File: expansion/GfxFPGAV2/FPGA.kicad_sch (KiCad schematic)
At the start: 26 parts, among them J1 JTAG, U2 XC6SLX9-FTG256, U302 W25Q64JVSSIM, Y1 ECS-3963

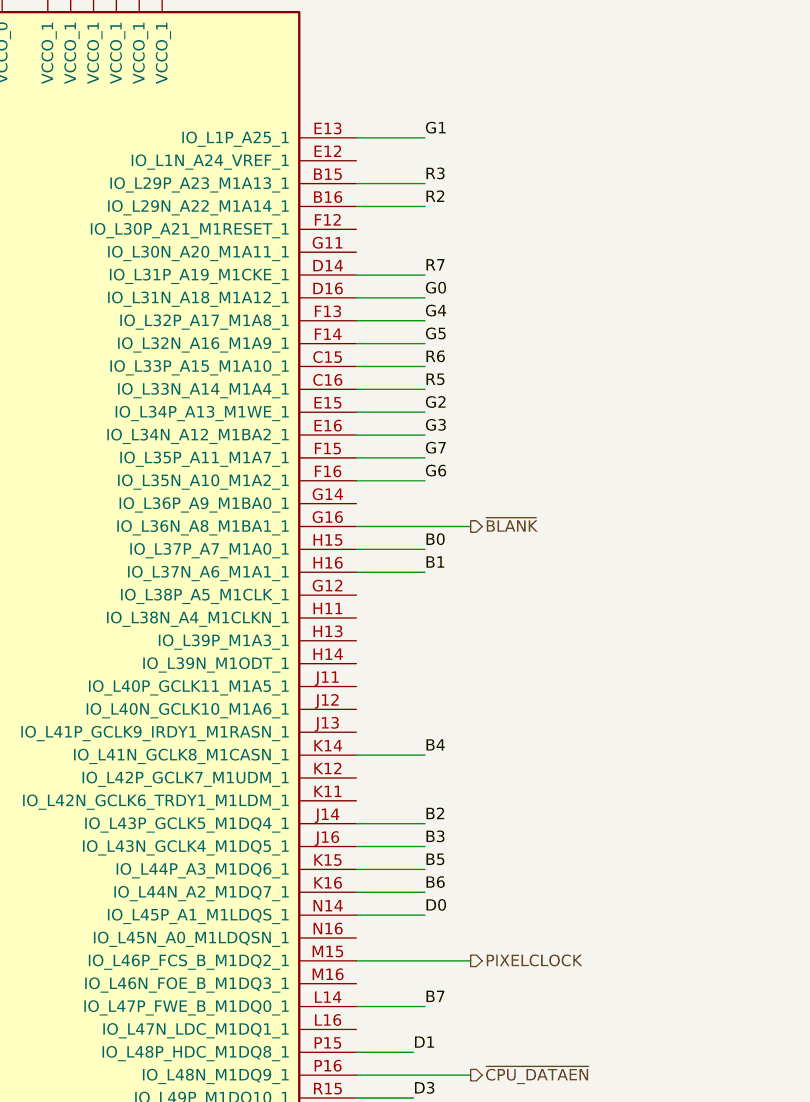
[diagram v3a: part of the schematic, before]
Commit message: Working on VGA baord layout
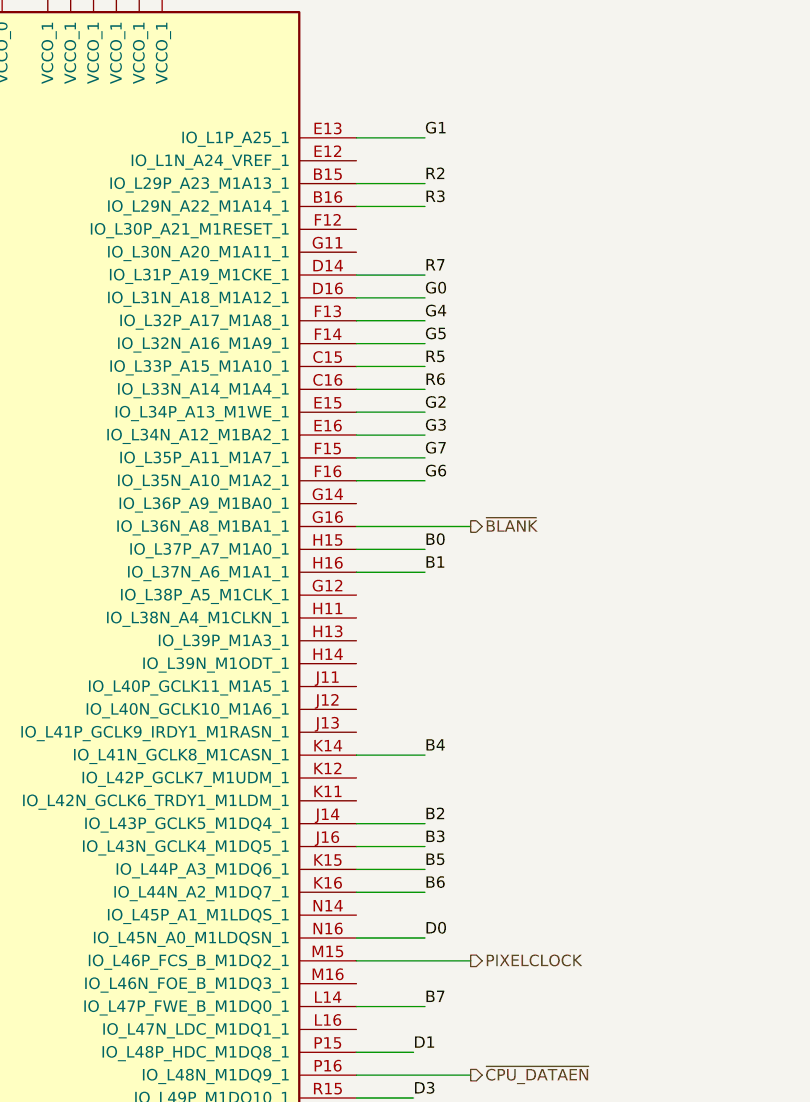
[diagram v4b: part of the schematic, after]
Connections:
- net D0: now also U2.N16 (IO_L45N_A0_M1LDQSN_1); no longer U2.N14 (IO_L45P_A1_M1LDQS_1)
- net R2: now also U2.B15 (IO_L29P_A23_M1A13_1); no longer U2.B16 (IO_L29N_A22_M1A14_1)
- net R3: now also U2.B16 (IO_L29N_A22_M1A14_1); no longer U2.B15 (IO_L29P_A23_M1A13_1)
- net R5: now also U2.C15 (IO_L33P_A15_M1A10_1); no longer U2.C16 (IO_L33N_A14_M1A4_1)
- net R6: now also U2.C16 (IO_L33N_A14_M1A4_1); no longer U2.C15 (IO_L33P_A15_M1A10_1)
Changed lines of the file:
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@@
 	(wire
 		(pts
-			(xy 152.4 130.81) (xy 144.78 130.81)
+			(xy 152.4 133.35) (xy 144.78 133.35)
 		)
 		(stroke
@@
 	)
 	(label "R2"
-		(at 152.4 52.07 0)
+		(at 152.4 49.53 0)
 		(fields_autoplaced yes)
 		(effects
@@
 	)
 	(label "R6"
-		(at 152.4 69.85 0)
+		(at 152.4 72.39 0)
 		(fields_autoplaced yes)
 		(effects
@@
 	)
 	(label "R3"
-		(at 152.4 49.53 0)
+		(at 152.4 52.07 0)
 		(fields_autoplaced yes)
 		(effects
@@
 	)
 	(label "D0"
-		(at 152.4 130.81 0)
+		(at 152.4 133.35 0)
 		(fields_autoplaced yes)
 		(effects
@@
 	)
 	(label "R5"
-		(at 152.4 72.39 0)
+		(at 152.4 69.85 0)
 		(fields_autoplaced yes)
 		(effects

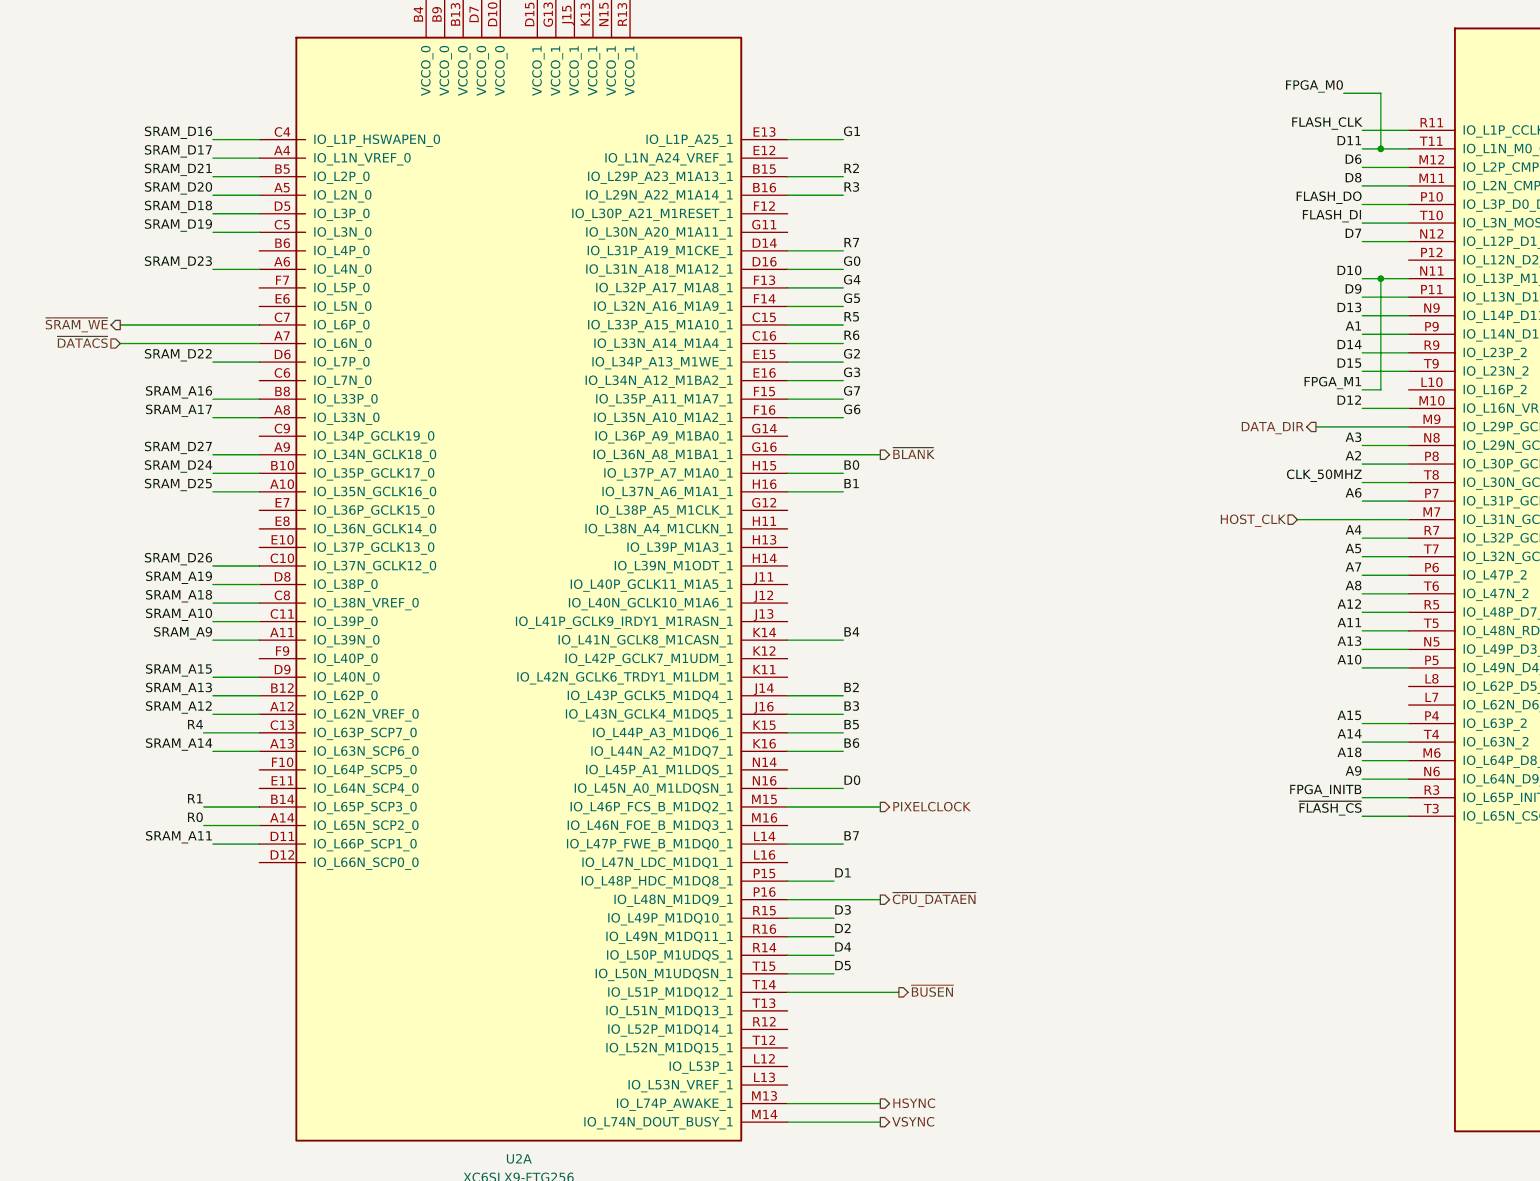
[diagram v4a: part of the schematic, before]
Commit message: More routing on the VGA board
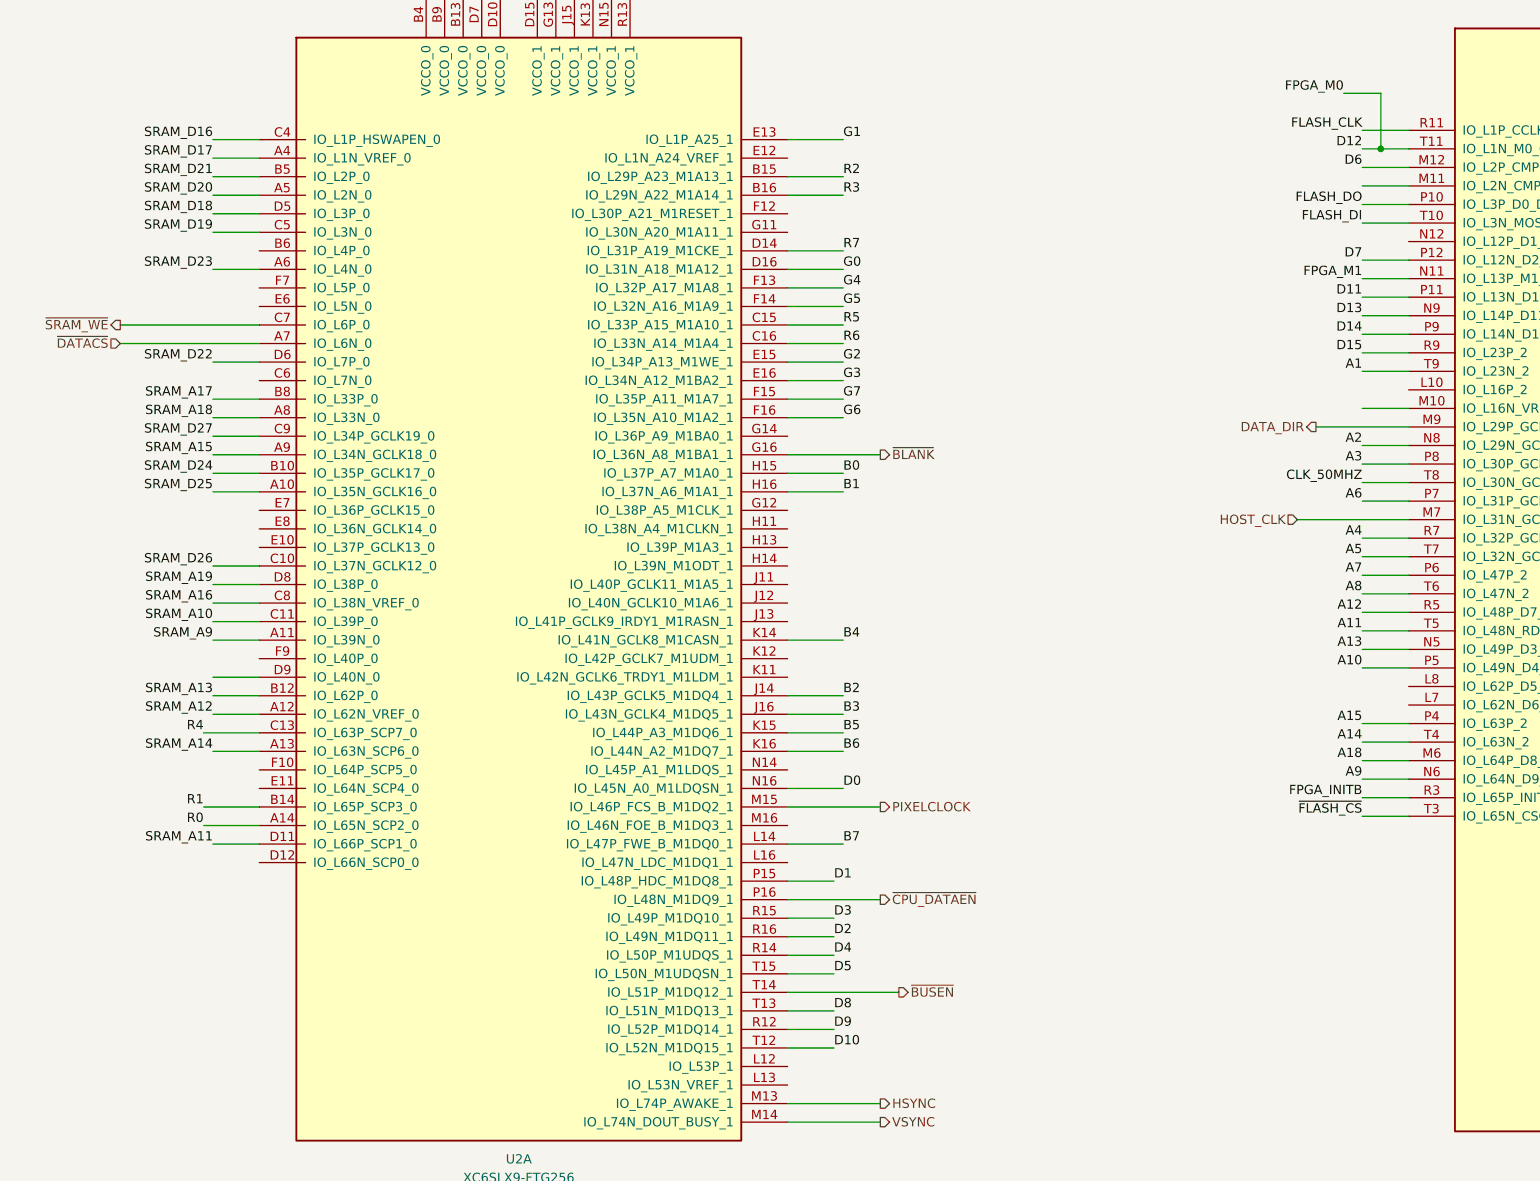
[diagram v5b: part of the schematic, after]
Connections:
- net A1: now also U2.T9 (IO_L23N_2); no longer U2.P9 (IO_L14N_D12_2)
- net A2: now also U2.N8 (IO_L29N_GCLK2_2); no longer U2.P8 (IO_L30P_GCLK1_D13_2)
- net A3: now also U2.P8 (IO_L30P_GCLK1_D13_2); no longer U2.N8 (IO_L29N_GCLK2_2)
- net D10: now also U2.T12 (IO_L52N_M1DQ15_1); no longer R1.1, U2.N11 (IO_L13P_M1_2)
- net D11: now also U2.P11 (IO_L13N_D10_2); no longer R4.2, U2.T11 (IO_L1N_M0_CMPMISO_2)
- net D12: now also R4.2, U2.T11 (IO_L1N_M0_CMPMISO_2); no longer U2.M10 (IO_L16N_VREF_2)
- net D14: now also U2.P9 (IO_L14N_D12_2); no longer U2.R9 (IO_L23P_2)
- net D15: now also U2.R9 (IO_L23P_2); no longer U2.T9 (IO_L23N_2)
- net D7: now also U2.P12 (IO_L12N_D2_MISO3_2); no longer U2.N12 (IO_L12P_D1_MISO2_2)
- net D8: now also U2.T13 (IO_L51N_M1DQ13_1); no longer U2.M11 (IO_L2N_CMPMOSI_2)
- net D9: now also U2.R12 (IO_L52P_M1DQ14_1); no longer U2.P11 (IO_L13N_D10_2)
- net SRAM_A15: now also U2.A9 (IO_L34N_GCLK18_0); no longer U2.D9 (IO_L40N_0)
- net SRAM_A16: now also U2.C8 (IO_L38N_VREF_0); no longer U2.B8 (IO_L33P_0)
- net SRAM_A17: now also U2.B8 (IO_L33P_0); no longer U2.A8 (IO_L33N_0)
- net SRAM_A18: now also U2.A8 (IO_L33N_0); no longer U2.C8 (IO_L38N_VREF_0)
- net SRAM_D27: now also U2.C9 (IO_L34P_GCLK19_0); no longer U2.A9 (IO_L34N_GCLK18_0)
- new net FPGA_M1: R1.1, U2.N11 (IO_L13P_M1_2)
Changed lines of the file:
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@@
 	)
 	(junction
-		(at 226.06 63.5)
-		(diameter 0)
-		(color 0 0 0 0)
-	)
-	(junction
 		(at 367.03 187.96)
 		(diameter 0)
@@
 	(wire
 		(pts
+			(xy 144.78 166.37) (xy 151.13 166.37)
+		)
+		(stroke
+			(width 0)
+			(type default)
+		)
+	)
+	(wire
+		(pts
 			(xy 261.62 20.32) (xy 264.16 20.32)
 		)
@@
 	(wire
 		(pts
-			(xy 226.06 63.5) (xy 229.87 63.5)
+			(xy 223.52 63.5) (xy 229.87 63.5)
 		)
 		(stroke
@@
 	(wire
 		(pts
-			(xy 226.06 63.5) (xy 226.06 78.74)
-		)
-		(stroke
-			(width 0)
-			(type default)
-		)
-	)
-	(wire
-		(pts
 			(xy 229.87 91.44) (xy 223.52 91.44)
 		)
@@
 	(wire
 		(pts
-			(xy 223.52 58.42) (xy 229.87 58.42)
+			(xy 223.52 60.96) (xy 229.87 60.96)
 		)
 		(stroke
@@
 	(wire
 		(pts
+			(xy 144.78 168.91) (xy 151.13 168.91)
+		)
+		(stroke
+			(width 0)
+			(type default)
+		)
+	)
+	(wire
+		(pts
 			(xy 144.78 179.07) (xy 157.48 179.07)
 		)
@@
 	(wire
 		(pts
-			(xy 223.52 63.5) (xy 226.06 63.5)
-		)
-		(stroke
-			(width 0)
-			(type default)
-		)
-	)
-	(wire
-		(pts
 			(xy 303.53 167.64) (xy 309.88 167.64)
 		)
@@
 	(wire
 		(pts
+			(xy 66.04 85.09) (xy 72.39 85.09)
+		)
+		(stroke
+			(width 0)
+			(type default)
+		)
+	)
+	(wire
+		(pts
 			(xy 373.38 82.55) (xy 382.27 82.55)
 		)
@@
 	(wire
 		(pts
+			(xy 144.78 163.83) (xy 151.13 163.83)
+		)
+		(stroke
+			(width 0)
+			(type default)
+		)
+	)
+	(wire
+		(pts
 			(xy 40.64 255.27) (xy 43.18 255.27)
 		)
@@
 	(wire
 		(pts
-			(xy 223.52 78.74) (xy 226.06 78.74)
-		)
-		(stroke
-			(width 0)
-			(type default)
-		)
-	)
-	(wire
-		(pts
 			(xy 256.54 20.32) (xy 256.54 22.86)
 		)
@@
 	)
 	(label "D9"
-		(at 223.52 66.04 180)
+		(at 151.13 166.37 0)
 		(fields_autoplaced yes)
 		(effects
@@
 				(size 1.27 1.27)
 			)
-			(justify right bottom)
+			(justify left bottom)
 		)
 	)
@@
 	)
 	(label "SRAM_A17"
-		(at 66.04 82.55 180)
+		(at 66.04 80.01 180)
 		(fields_autoplaced yes)
 		(effects
@@
 	)
 	(label "D15"
-		(at 223.52 76.2 180)
+		(at 223.52 73.66 180)
 		(fields_autoplaced yes)
 		(effects
@@
 	)
 	(label "SRAM_A18"
-		(at 66.04 107.95 180)
+		(at 66.04 82.55 180)
 		(fields_autoplaced yes)
 		(effects
@@
 	)
 	(label "D11"
-		(at 223.52 45.72 180)
+		(at 223.52 66.04 180)
 		(fields_autoplaced yes)
 		(effects
@@
 	)
 	(label "SRAM_A15"
-		(at 66.04 118.11 180)
+		(at 66.04 87.63 180)
 		(fields_autoplaced yes)
 		(effects
@@
 	)
 	(label "A2"
-		(at 223.52 88.9 180)
+		(at 223.52 86.36 180)
 		(fields_autoplaced yes)
 		(effects
@@
 	)
 	(label "D12"
-		(at 223.52 81.28 180)
+		(at 223.52 45.72 180)
 		(fields_autoplaced yes)
 		(effects
@@
 	)
 	(label "SRAM_D27"
-		(at 66.04 87.63 180)
+		(at 66.04 85.09 180)
 		(fields_autoplaced yes)
 		(effects
@@
 	)
 	(label "D14"
-		(at 223.52 73.66 180)
+		(at 223.52 71.12 180)
 		(fields_autoplaced yes)
 		(effects
@@
 	)
 	(label "FPGA_M1"
-		(at 223.52 78.74 180)
+		(at 223.52 63.5 180)
 		(fields_autoplaced yes)
 		(effects
@@
 	)
 	(label "D7"
-		(at 223.52 58.42 180)
+		(at 223.52 60.96 180)
 		(fields_autoplaced yes)
 		(effects
@@
 	)
 	(label "D8"
-		(at 223.52 50.8 180)
+		(at 151.13 163.83 0)
 		(fields_autoplaced yes)
 		(effects
@@
 				(size 1.27 1.27)
 			)
-			(justify right bottom)
+			(justify left bottom)
 		)
 	)
@@
 	)
 	(label "D10"
-		(at 223.52 63.5 180)
+		(at 151.13 168.91 0)
 		(fields_autoplaced yes)
 		(effects
@@
 				(size 1.27 1.27)
 			)
-			(justify right bottom)
+			(justify left bottom)
 		)
 	)
@@
 	)
 	(label "SRAM_A16"
-		(at 66.04 80.01 180)
+		(at 66.04 107.95 180)
 		(fields_autoplaced yes)
 		(effects
@@
 	)
 	(label "A3"
-		(at 223.52 86.36 180)
+		(at 223.52 88.9 180)
 		(fields_autoplaced yes)
 		(effects
@@
 	)
 	(label "A1"
-		(at 223.52 71.12 180)
+		(at 223.52 76.2 180)
 		(fields_autoplaced yes)
 		(effects
